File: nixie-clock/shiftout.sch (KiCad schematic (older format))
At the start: 24 parts, among them U10 74HC595, U11 74141, U12 74141, U4 74HC595, U5 74141, U6 74141, U7 74HC595, U8 74141, U9 74141

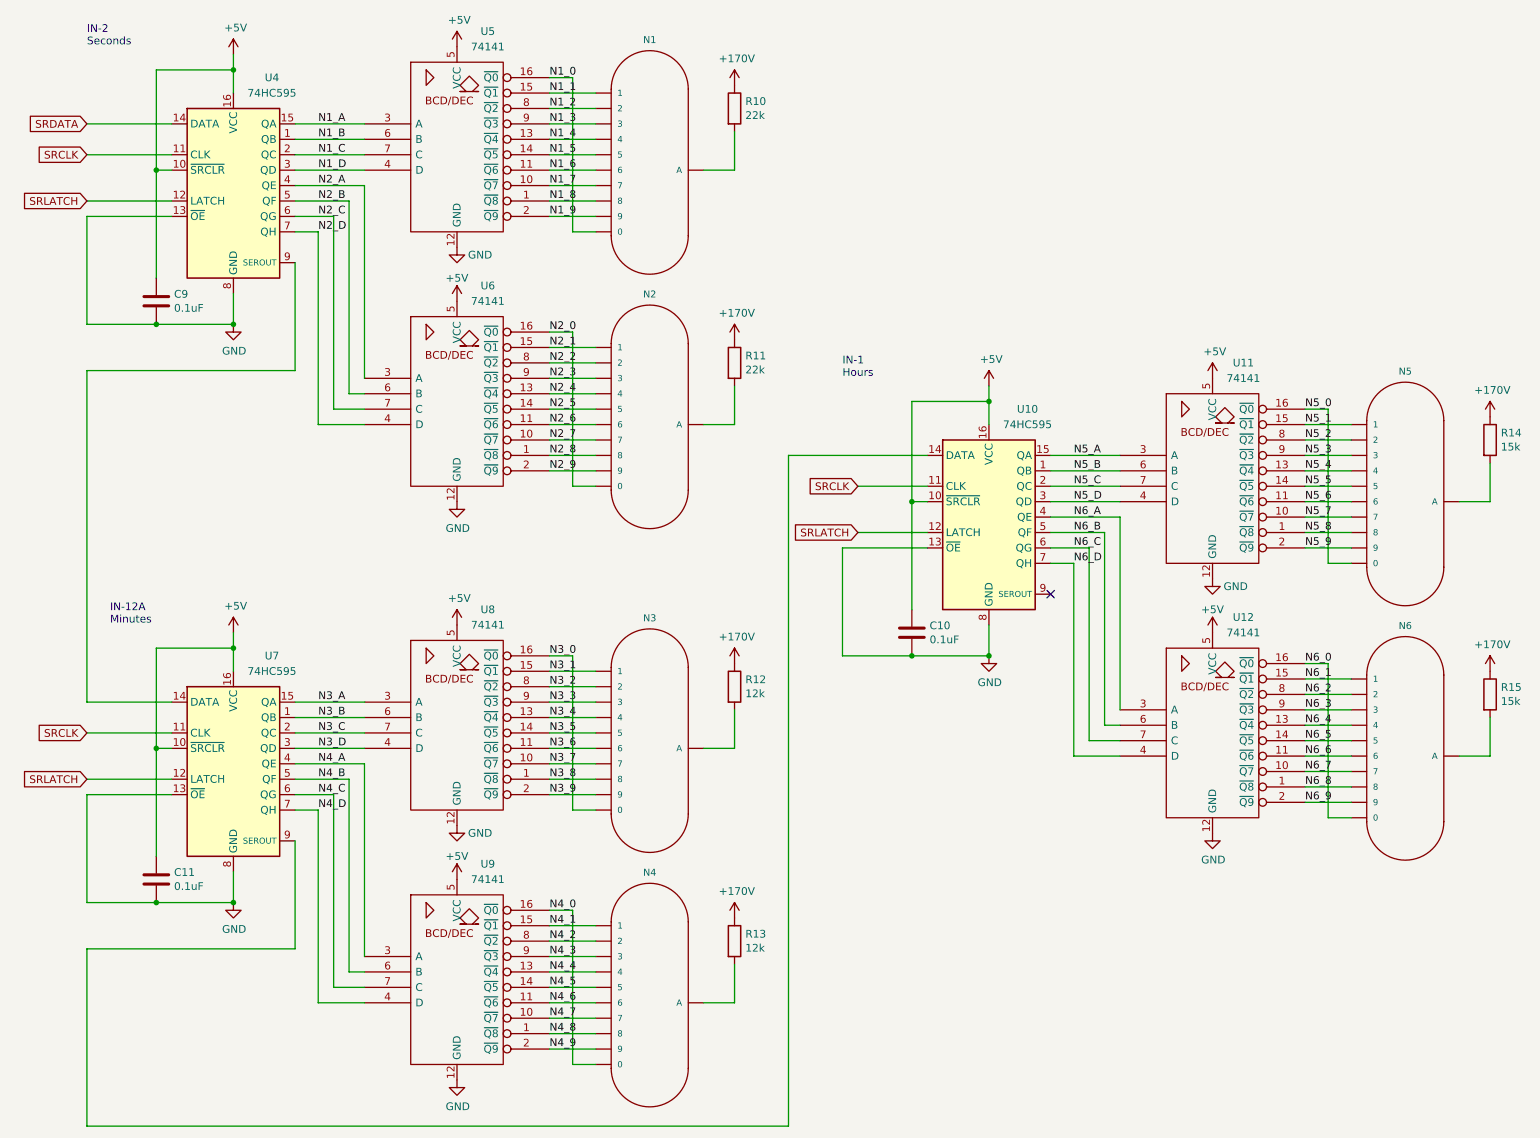
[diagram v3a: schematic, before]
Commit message: Fixed anode net names. Finished routing anode connections.
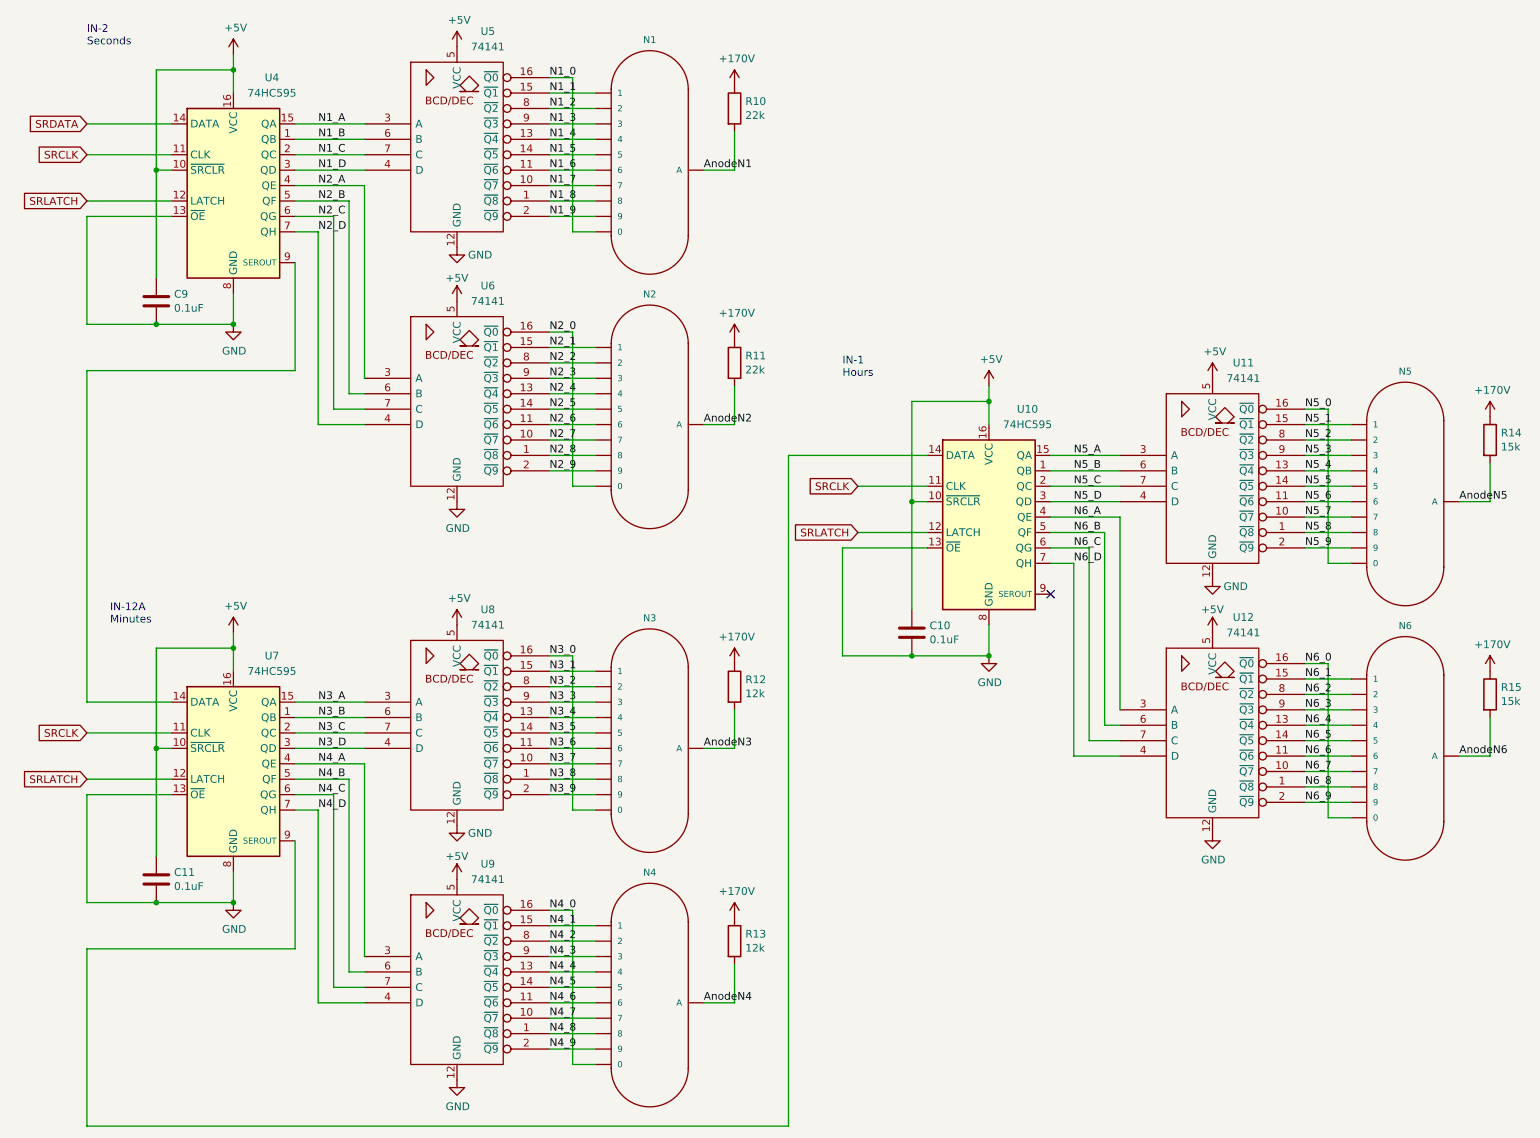
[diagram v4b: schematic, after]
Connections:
- net AnodeN1: now reaches N1.A, R10.2
- net AnodeN2: now reaches N2.A, R11.2
- net AnodeN3: now reaches N3.A, R12.2
- net AnodeN4: now reaches N4.A, R13.2
- net AnodeN5: now reaches N5.A, R14.2
- net AnodeN6: now reaches N6.A, R15.2
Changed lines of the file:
@@
 Text Label 8850 5750 0    50   ~ 0
 N6_9
+Text Label 4950 1650 0    50   ~ 0
+AnodeN1
+Text Label 4950 3300 0    50   ~ 0
+AnodeN2
+Text Label 4950 5400 0    50   ~ 0
+AnodeN3
+Text Label 4950 7050 0    50   ~ 0
+AnodeN4
+Text Label 9850 3800 0    50   ~ 0
+AnodeN5
+Text Label 9850 5450 0    50   ~ 0
+AnodeN6
 $EndSCHEMATC
